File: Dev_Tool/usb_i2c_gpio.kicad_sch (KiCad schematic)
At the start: 24 parts, among them J10 Conn_02x02_Odd_Even, J11 Conn_01x01_Pin, J3 Conn_01x04, U21 SN74LVC1G07DBV, U22 SN74LVC1G07DBV, U4 MCP2221A-I/ST, U5 PCA9535PW

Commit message: Final tweaks before ordering PCBs
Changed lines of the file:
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@@
 	(text "IN_USE"
 		(exclude_from_sim no)
-		(at 220.98 93.98 0)
+		(at 233.68 93.98 0)
 		(effects
 			(font

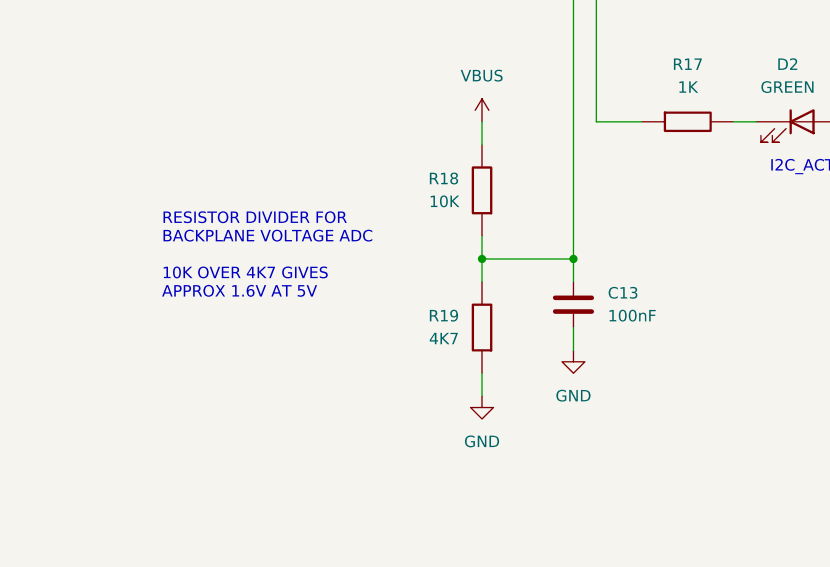
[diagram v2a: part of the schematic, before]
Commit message: Add unconnected pins to CPLD symbol
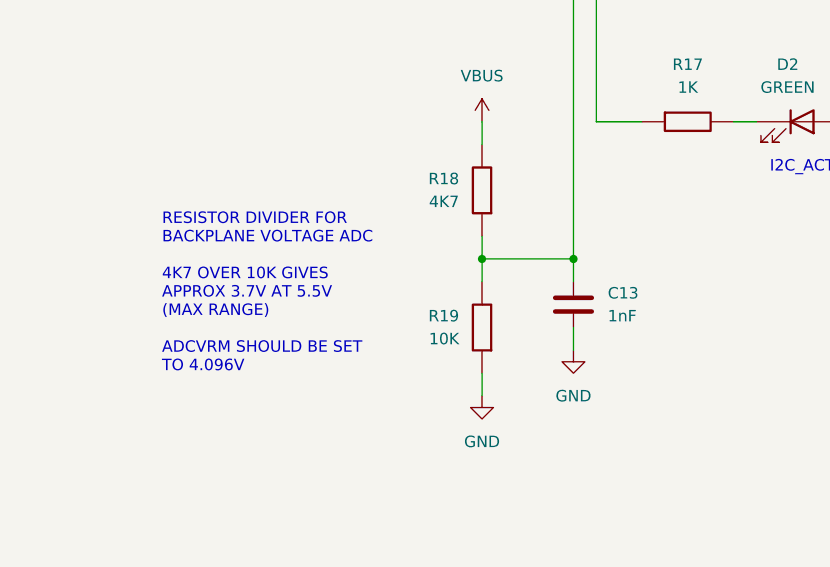
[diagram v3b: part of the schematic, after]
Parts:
- C13: value 100nF -> 1nF
- R18: value 10K -> 4K7
- R19: value 4K7 -> 10K
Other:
- note added: "RESISTOR DIVIDER FOR BACKPLANE VOLTAGE ADC 4K7 OVER 10K GIVES APPROX 3.7V AT 5.5V (MAX RANGE) ADCVRM SHOULD BE SET TO 4.096V"
- note removed: "RESISTOR DIVIDER FOR BACKPLANE VOLTAGE ADC 10K OVER 4K7 GIVES APPROX 1.6V AT 5V"
- title: USB-I2C CONVERTER AND I2C GPIO EXPANDER -> USB-I2C CONVERTER AND I2C GPIO EXPANDER (PORT C)
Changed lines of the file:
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@@
 	(paper "A4")
 	(title_block
-		(title "USB-I2C CONVERTER AND I2C GPIO EXPANDER")
-		(date "2025-09-08")
+		(title "USB-I2C CONVERTER AND I2C GPIO EXPANDER (PORT C)")
+		(date "2025-09-09")
 		(rev "1")
 		(company "(C) TOM STOREY")
@@
 		)
 	)
-	(text "RESISTOR DIVIDER FOR\nBACKPLANE VOLTAGE ADC\n\n10K OVER 4K7 GIVES\nAPPROX 1.6V AT 5V"
+	(text "RESISTOR DIVIDER FOR\nBACKPLANE VOLTAGE ADC\n\n4K7 OVER 10K GIVES\nAPPROX 3.7V AT 5.5V\n(MAX RANGE)\n\nADCVRM SHOULD BE SET\nTO 4.096V"
 		(exclude_from_sim no)
 		(at 38.1 101.6 0)
@@
 			)
 		)
-		(property "Value" "100nF"
+		(property "Value" "1nF"
 			(at 87.63 113.0299 0)
 			(effects
@@
 			)
 		)
-		(property "Value" "10K"
+		(property "Value" "4K7"
 			(at 71.12 100.3299 0)
 			(effects
@@
 			)
 		)
-		(property "Value" "4K7"
+		(property "Value" "10K"
 			(at 71.12 115.5699 0)
 			(effects

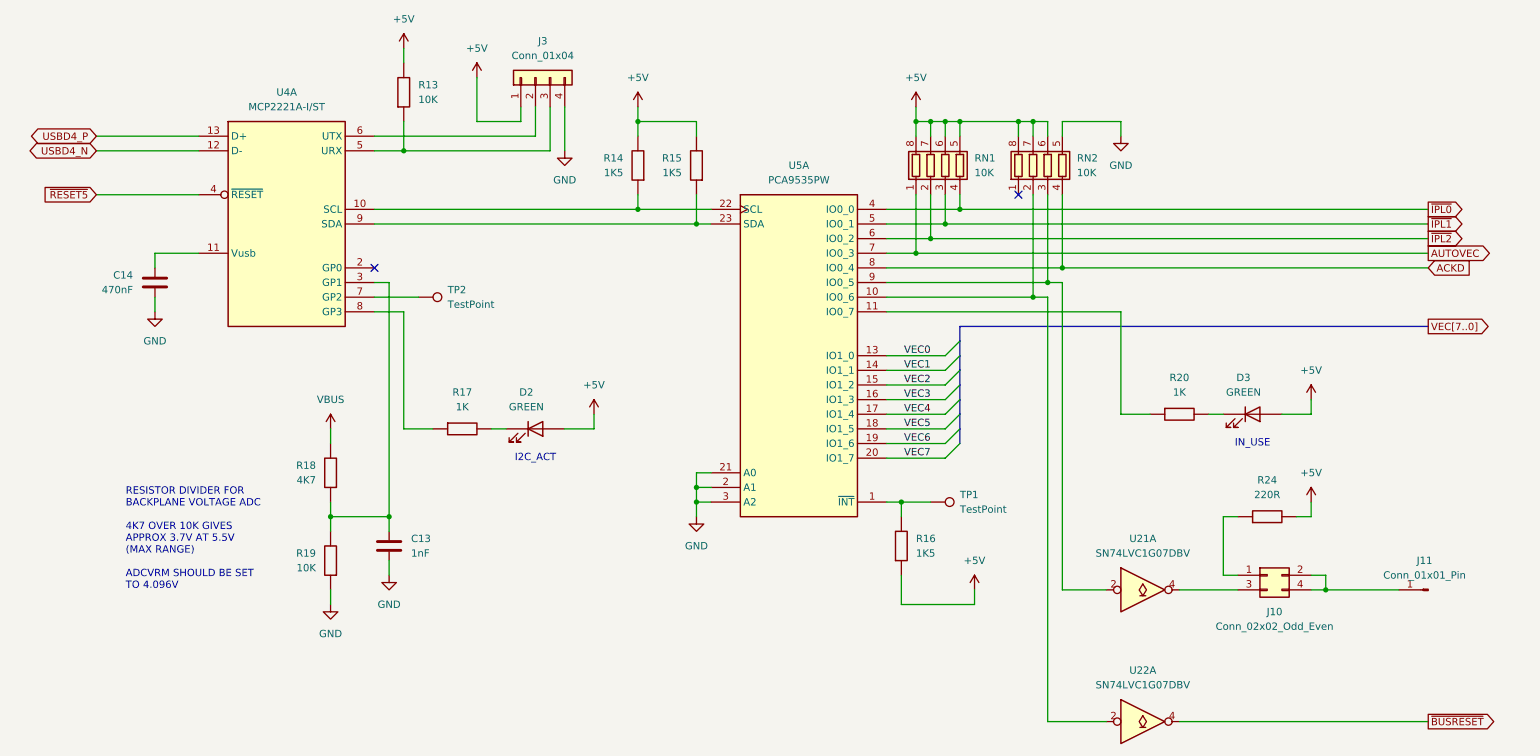
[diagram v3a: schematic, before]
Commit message: Rev 2 fixes
* R5/C1 reference silkscreens were swapped around
* LED logic for the PC LED was reverse to what I thought it would be, fixed by adding Q1
* Change DEV LED to PWR ON LED, since it comes on when the port is powered, not just when a device is connected. Switched via Q2 so it doesnt fade on power down.
* IN USE LED now comes off MCP2221A pin - the PCA9535 doesnt have a reset, so this LED could remain lit even after a reset.
* Pull up/down added to vector buffer
* 8P8C sockets moved further out as they are shorter than the footprint suggests
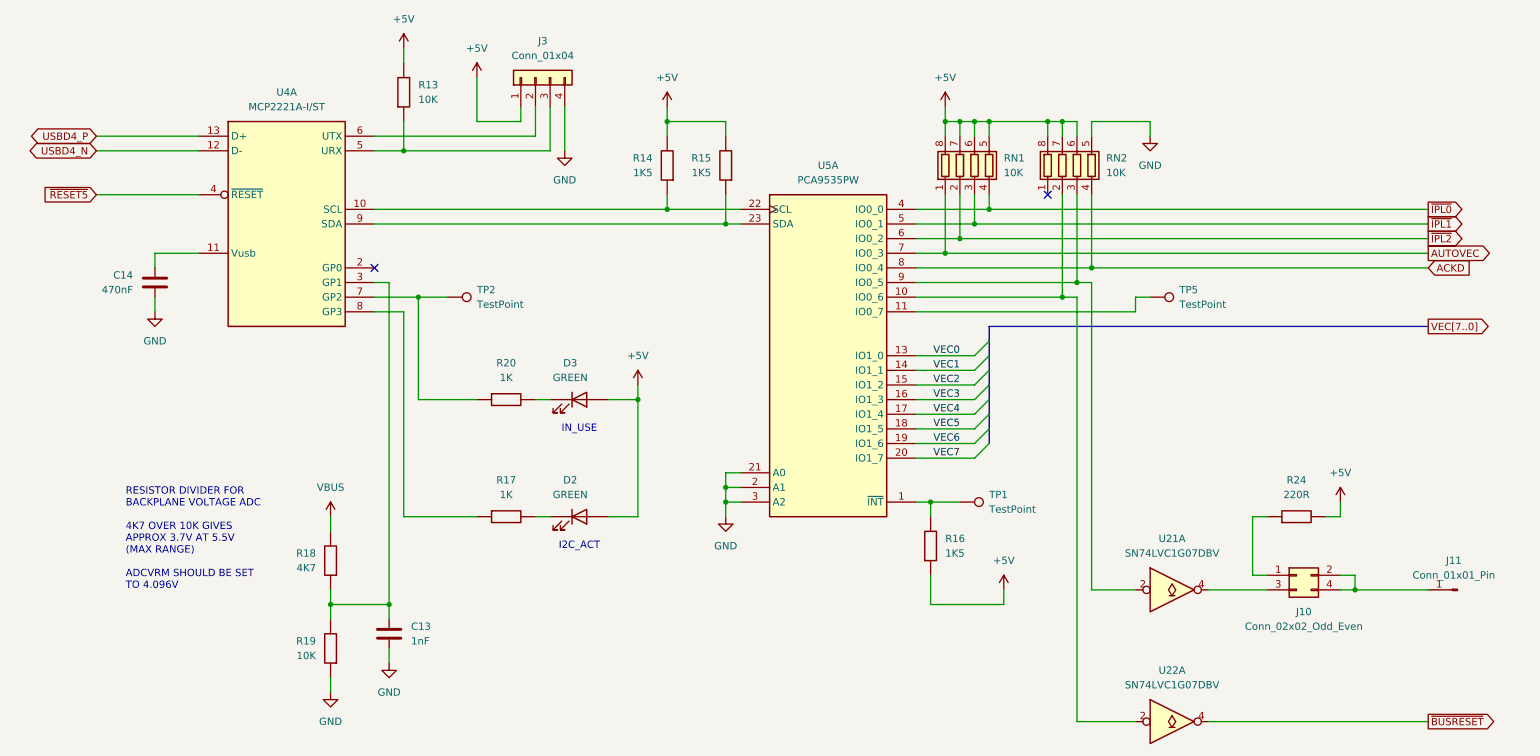
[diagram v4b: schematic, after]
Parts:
- added TP5: TestPoint, TestPoint:TestPoint_Pad_D1.5mm, symbol Connector:TestPoint
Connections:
- net at TP2.1, U4.7 (GP2): now also R20.2
- net at U5.11 (IO0_7): now also TP5.1; no longer R20.2
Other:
- moved on the sheet: C13, D2, D3, J10, J11, R14, R15, R16, R17, R18, R19, R20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

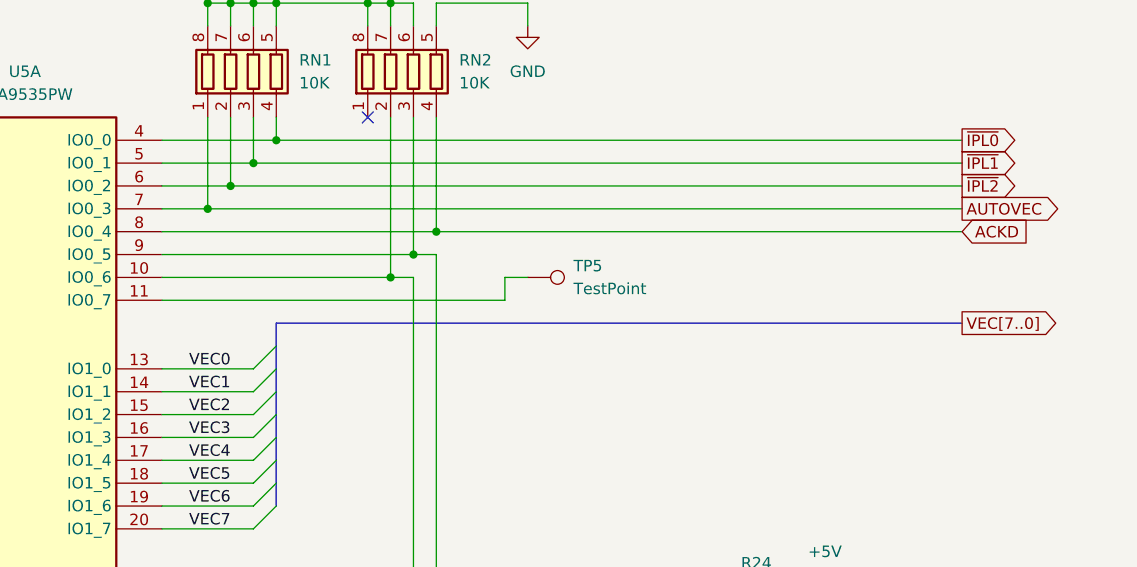
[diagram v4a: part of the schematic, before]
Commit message: Further changes for rev 2
* Since the IN USE LED was moved to the MCP2221A, this freed up a GPIO on the PCA9535. Connect this to the SYSRESET signal so that it can be monitored during reset operations
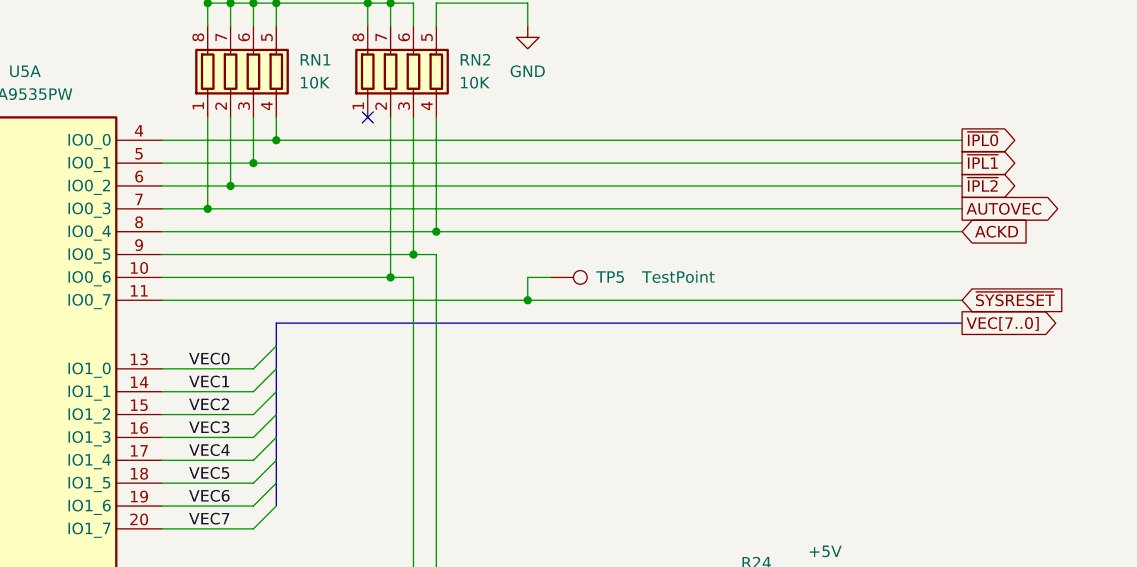
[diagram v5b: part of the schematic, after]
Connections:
- net ~{SYSRESET}: now reaches TP5.1, U5.11 (IO0_7)
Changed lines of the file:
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@@
 	(title_block
 		(title "USB-I2C CONVERTER AND I2C GPIO EXPANDER (PORT C)")
-		(date "2025-09-18")
+		(date "2025-09-21")
 		(rev "2")
 		(company "(C) TOM STOREY")
@@
 	)
 	(junction
+		(at 215.9 71.12)
+		(diameter 0)
+		(color 0 0 0 0)
+	)
+	(junction
 		(at 200.66 38.1)
 		(diameter 0)
@@
 	(wire
 		(pts
-			(xy 213.36 68.58) (xy 213.36 71.12)
-		)
-		(stroke
-			(width 0)
-			(type default)
-		)
-	)
-	(wire
-		(pts
 			(xy 198.12 38.1) (xy 200.66 38.1)
 		)
@@
 		)
 	)
+	(wire
+		(pts
+			(xy 218.44 68.58) (xy 215.9 68.58)
+		)
+		(stroke
+			(width 0)
+			(type default)
+		)
+	)
 	(bus
 		(pts
@@
 	(wire
 		(pts
-			(xy 175.26 71.12) (xy 213.36 71.12)
+			(xy 175.26 71.12) (xy 215.9 71.12)
 		)
 		(stroke
@@
 	(wire
 		(pts
+			(xy 215.9 68.58) (xy 215.9 71.12)
+		)
+		(stroke
+			(width 0)
+			(type default)
+		)
+	)
+	(wire
+		(pts
 			(xy 187.96 53.34) (xy 264.16 53.34)
 		)
@@
 	(wire
 		(pts
-			(xy 213.36 68.58) (xy 215.9 68.58)
-		)
-		(stroke
-			(width 0)
-			(type default)
-		)
-	)
-	(wire
-		(pts
 			(xy 114.3 35.56) (xy 114.3 43.18)
 		)
@@
 		(pts
 			(xy 86.36 106.68) (xy 99.06 106.68)
+		)
+		(stroke
+			(width 0)
+			(type default)
+		)
+	)
+	(wire
+		(pts
+			(xy 215.9 71.12) (xy 264.16 71.12)
 		)
 		(stroke
@@
 		(property "Intersheetrefs" "${INTERSHEET_REFS}"
 			(at 275.9748 73.66 0)
+			(effects
+				(font
+					(size 1.27 1.27)
+				)
+				(justify left)
+				(hide yes)
+			)
+		)
+	)
+	(global_label "~{SYSRESET}"
+		(shape input)
+		(at 264.16 71.12 0)
+		(fields_autoplaced yes)
+		(effects
+			(font
+				(size 1.27 1.27)
+			)
+			(justify left)
+		)
+		(property "Intersheetrefs" "${INTERSHEET_REFS}"
+			(at 276.3979 71.12 0)
 			(effects
 				(font
@@
 	)
 	(symbol
+		(lib_id "Connector:TestPoint")
+		(at 218.44 68.58 270)
+		(unit 1)
+		(exclude_from_sim no)
+		(in_bom yes)
+		(on_board yes)
+		(dnp no)
+		(property "Reference" "TP5"
+			(at 223.52 68.58 90)
+			(effects
+				(font
+					(size 1.27 1.27)
+				)
+				(justify left)
+			)
+		)
+		(property "Value" "TestPoint"
+			(at 228.6 68.58 90)
+			(effects
+				(font
+					(size 1.27 1.27)
+				)
+				(justify left)
+			)
+		)
+		(property "Footprint" "TestPoint:TestPoint_Pad_D1.5mm"
+			(at 218.44 73.66 0)
+			(effects
+				(font
+					(size 1.27 1.27)
+				)
+				(hide yes)
+			)
+		)
+		(property "Datasheet" "~"
+			(at 218.44 73.66 0)
+			(effects
+				(font
+					(size 1.27 1.27)
+				)
+				(hide yes)
+			)
+		)
+		(property "Description" "test point"
+			(at 218.44 68.58 0)
+			(effects
+				(font
+					(size 1.27 1.27)
+				)
+				(hide yes)
+			)
+		)
+		(pin "1"
+		)
+		(instances
+			(project "Dev_Tool"
+				(path "/a5cc9727-587c-40e3-bd55-82381bb9520b/b4fc2b01-933f-4ccf-b6d4-7f874139b255"
+					(reference "TP5")
+					(unit 1)
+				)
+			)
+		)
+	)
+	(symbol
 		(lib_id "COMET_symbols:C")
 		(at 83.82 127 0)
@@
 					(unit 1)
 				)
-			)
-		)
-	)
-	(symbol
-		(lib_id "Connector:TestPoint")
-		(at 215.9 68.58 270)
-		(unit 1)
-		(exclude_from_sim no)
-		(in_bom yes)
-		(on_board yes)
-		(dnp no)
-		(fields_autoplaced yes)
-		(property "Reference" "TP5"
-			(at 220.98 67.3099 90)
-			(effects
-				(font
-					(size 1.27 1.27)
-				)
-				(justify left)
-			)
-		)
-		(property "Value" "TestPoint"
-			(at 220.98 69.8499 90)
-			(effects
-				(font
-					(size 1.27 1.27)
-				)
-				(justify left)
-			)
-		)
-		(property "Footprint" "TestPoint:TestPoint_Pad_D1.5mm"
-			(at 215.9 73.66 0)
-			(effects
-				(font
-					(size 1.27 1.27)
-				)
-				(hide yes)
-			)
-		)
-		(property "Datasheet" "~"
-			(at 215.9 73.66 0)
-			(effects
-				(font
-					(size 1.27 1.27)
-				)
-				(hide yes)
-			)
-		)
-		(property "Description" "test point"
-			(at 215.9 68.58 0)
-			(effects
-				(font
-					(size 1.27 1.27)
-				)
-				(hide yes)
-			)
-		)
-		(pin "1"
-		)
-		(instances
-			(project "Dev_Tool"
-				(path "/a5cc9727-587c-40e3-bd55-82381bb9520b/b4fc2b01-933f-4ccf-b6d4-7f874139b255"
-					(reference "TP5")
-					(unit 1)
-				)
